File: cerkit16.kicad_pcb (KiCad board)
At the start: 2 copper layers, 35 parts, among them U1 ProMicro

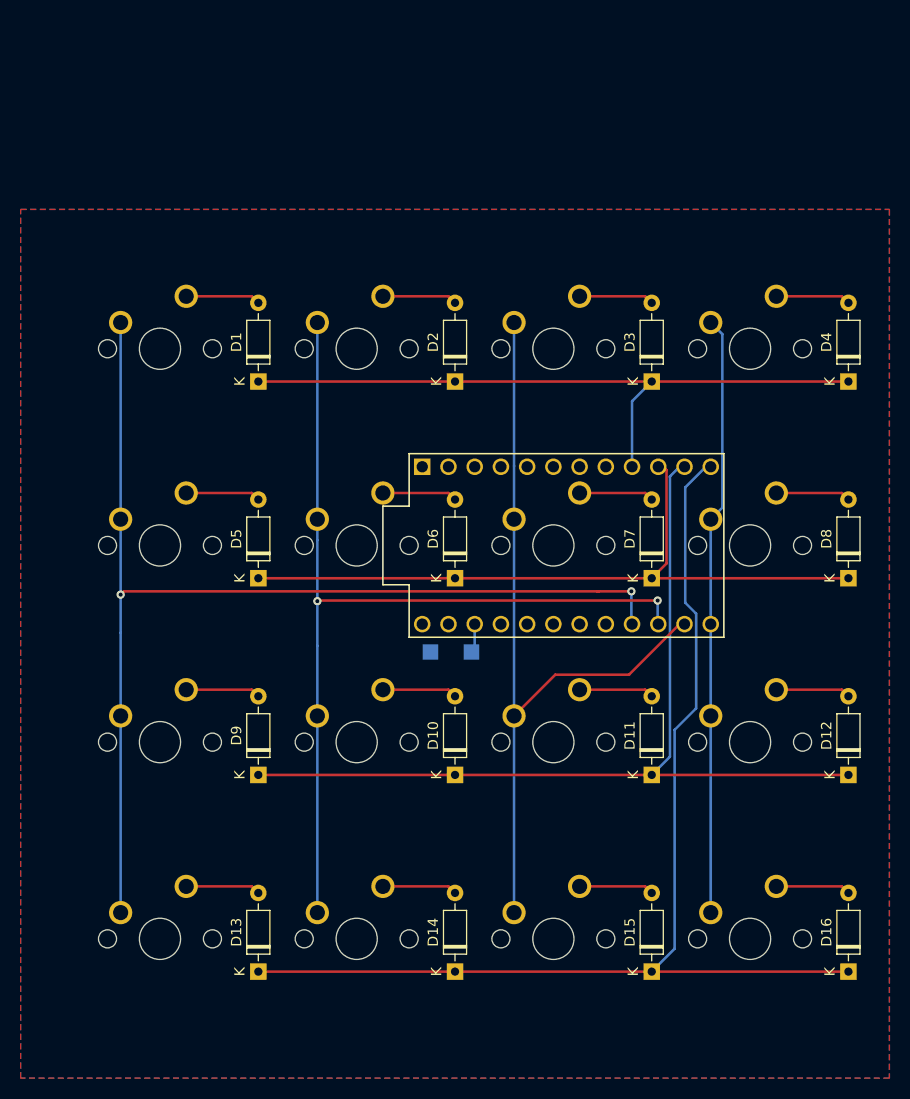
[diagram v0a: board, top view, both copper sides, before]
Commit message: moved the controller to the top of the board
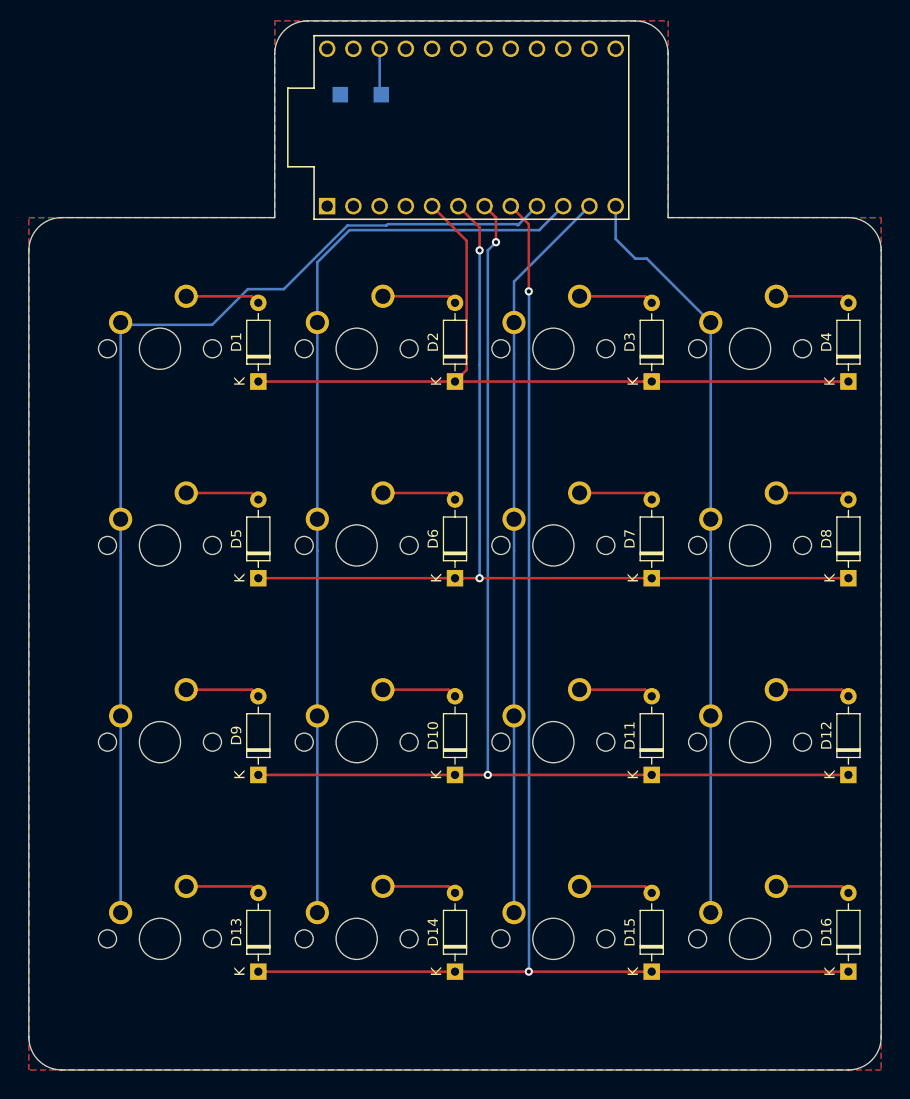
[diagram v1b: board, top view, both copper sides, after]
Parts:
- U1: moved to F.Cu
- moved RST1 54.7 mm to (66.7, 16.7)
- moved RST2 54.7 mm to (70.6, 16.7)
- moved U1 41.5 mm to (79.4, 19.8)
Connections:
- U1 pad 10: ROW1 -> COL1
- U1 pad 11: ROW2 -> COL2
- U1 pad 12: ROW3 -> COL3
- U1 pad 13: COL3 -> Net-(U1-Pad13)
- U1 pad 14: COL2 -> Net-(U1-Pad14)
- U1 pad 15: COL1 -> Net-(U1-Pad15)
- U1 pad 16: COL0 -> Net-(U1-Pad16)
- U1 pad 5: Net-(U1-Pad5) -> ROW0
- U1 pad 6: Net-(U1-Pad6) -> ROW1
- U1 pad 7: Net-(U1-Pad7) -> ROW2
- U1 pad 8: Net-(U1-Pad8) -> ROW3
- U1 pad 9: ROW0 -> COL0
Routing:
- net ROW1: track 69.3 -> 94.0 mm, vias 0 -> 2
- net ROW2: track 88.8 -> 113.0 mm, vias 0 -> 2
- net ROW3: track 109.8 -> 132.0 mm, vias 0 -> 2
- net COL3: track 58.1 -> 72.9 mm
- net ROW0: track 65.7 -> 76.0 mm
- net COL0: track 110.1 -> 102.5 mm, vias 2 -> 0
- net COL2: track 77.5 -> 71.4 mm
- net COL1: track 92.4 -> 89.1 mm, vias 2 -> 0
- net RST: track 3.31 -> 4.51 mm
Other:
- board outline added: 82.5 x 101.6 mm
